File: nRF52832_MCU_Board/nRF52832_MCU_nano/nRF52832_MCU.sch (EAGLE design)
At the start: 57 parts, among them J1 TSW-103-02-S-S, J2 TSW-116-02-S-S, J3 TSW-116-02-S-S, J4 TSW-103-02-S-S, J5 MICROUSB, J6 DEBUG_CONNECTOR, J7 FPC_05P-RA-SMD, J8 MM8130-2600, U1 NRF52832, U2 TLV1117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

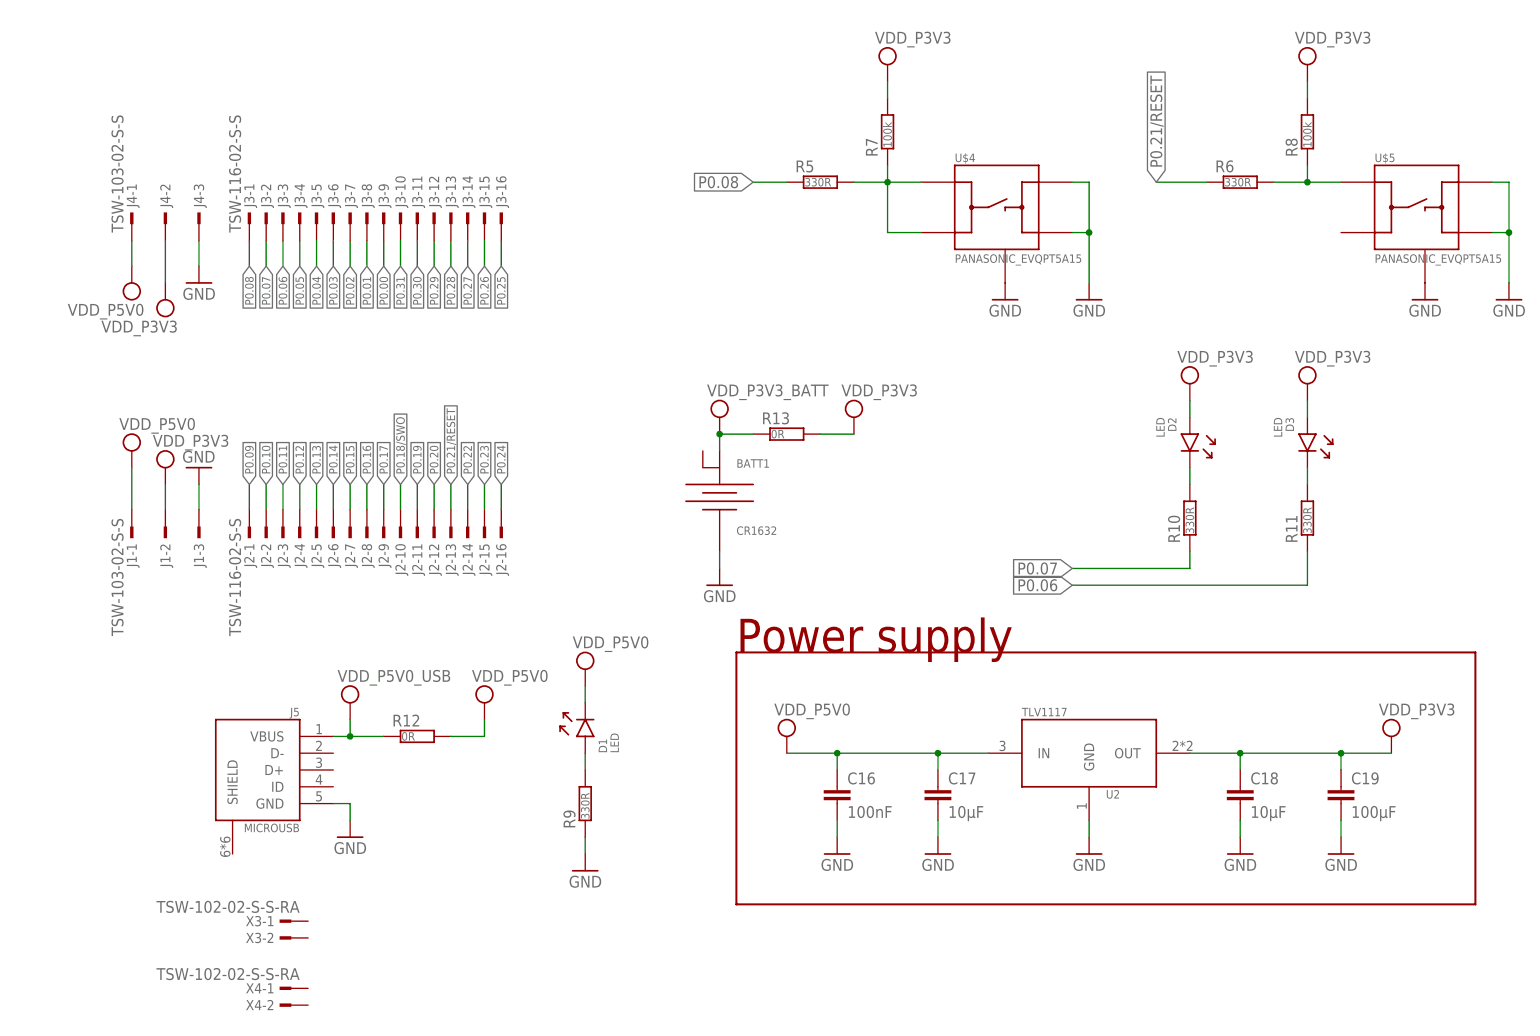
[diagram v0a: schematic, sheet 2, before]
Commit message: Cleaned up schematic
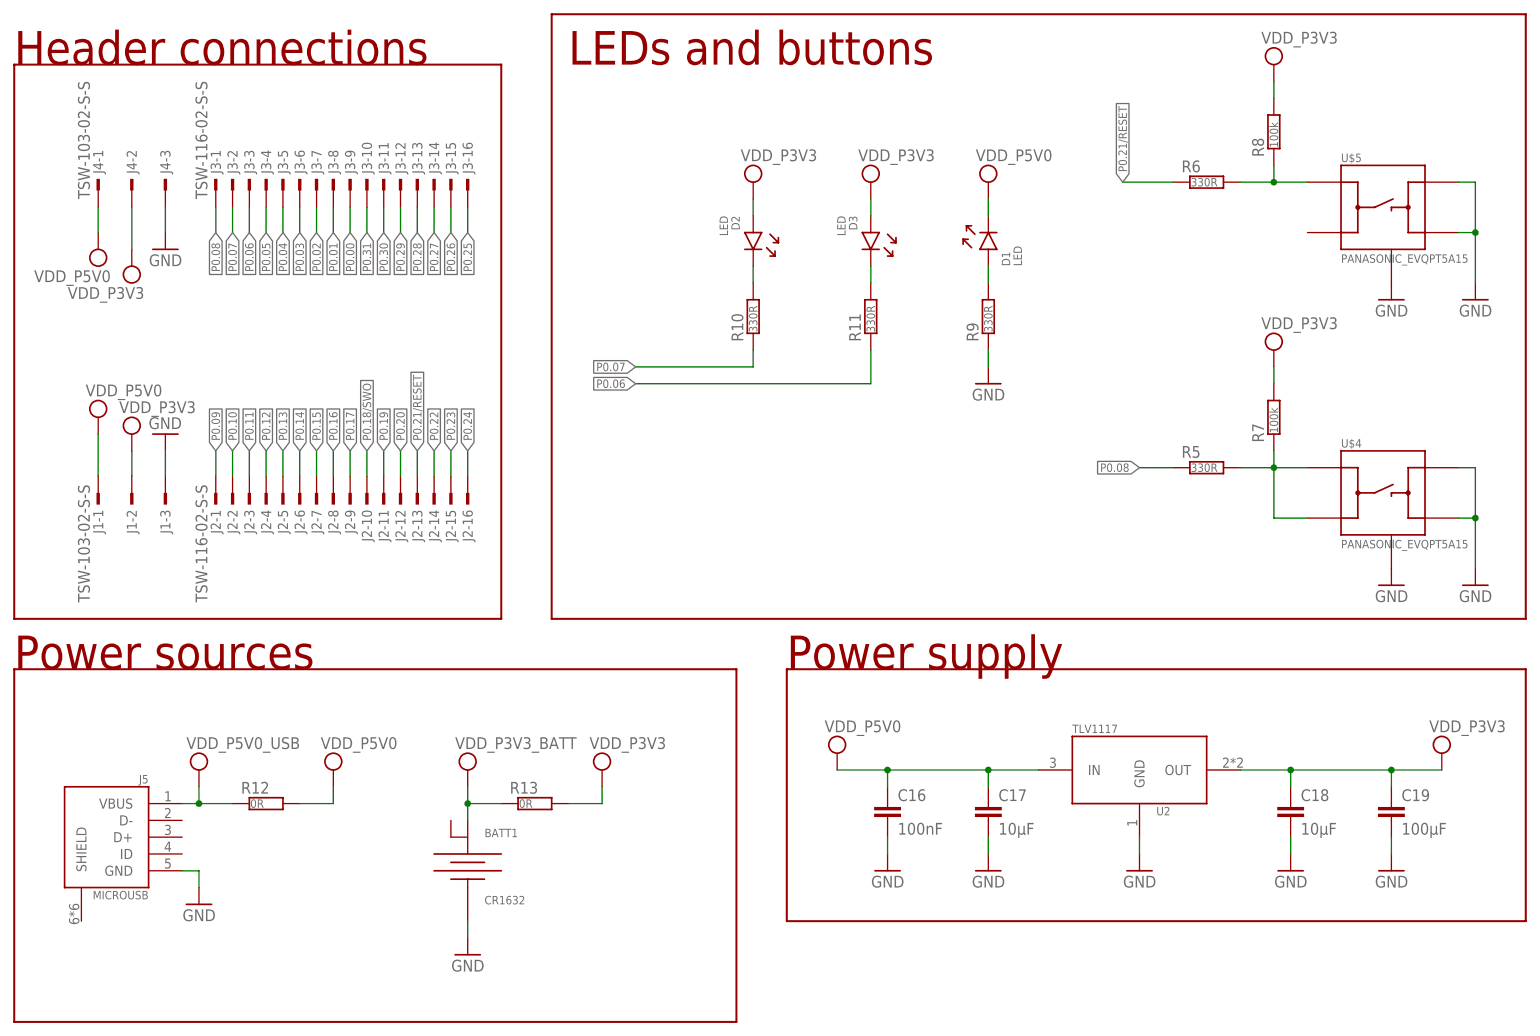
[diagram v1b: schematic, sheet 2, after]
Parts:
- removed X3, X4: TSW-102-02-S-S-RA, con-samtec:TSW-102-02-S-S-RA
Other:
- note added: "Header connections"
- note added: "LEDs and buttons"
- note added: "Power sources"
- moved on the sheet: BATT1, C16, C17, C18, C19, D1, D2, D3, J1-1, J1-2, J1-3, J2-1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
